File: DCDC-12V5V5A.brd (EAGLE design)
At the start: 40 x 23 mm, 32 parts, among them CN2 2828XX-2282834-2, CN3 2828XX-2282834-2, Q10 NMOSFET, Q9 NMOSFET, U1 LM3150MHX/NOPB

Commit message: Fixed some placement. Generated CAM files.
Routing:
- net 12V: track 15.4 -> 16.0 mm, vias 12 -> 13
- net GND: vias 36 -> 38
- net 5V: vias 17 -> 18
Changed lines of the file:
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@@
 <vertex x="13" y="20"/>
 <vertex x="15" y="20"/>
-<vertex x="15" y="22"/>
-<vertex x="9" y="22"/>
+<vertex x="15" y="21.7"/>
+<vertex x="9" y="21.7"/>
 <vertex x="9" y="17"/>
-<vertex x="7" y="15"/>
-<vertex x="2" y="15"/>
+<vertex x="6.5" y="14.5"/>
+<vertex x="2" y="14.5"/>
 <vertex x="2" y="12"/>
 <vertex x="3" y="12"/>
@@
 <vertex x="7" y="4"/>
 </polygon>
-<wire x1="18" y1="2.15" x2="17.55" y2="2.15" width="0.4064" layer="1"/>
-<wire x1="17.55" y1="2.15" x2="17.4" y2="2.3" width="0.4064" layer="1"/>
-<via x="17.4" y="2.3" extent="1-16" drill="0.35"/>
+<wire x1="18" y1="2.15" x2="17.15" y2="2.15" width="0.4064" layer="1"/>
+<wire x1="17.15" y1="2.15" x2="17.1" y2="2.2" width="0.4064" layer="1"/>
+<via x="17.1" y="2.2" extent="1-16" drill="0.35"/>
 <via x="14.2" y="5.7196375" extent="1-16" drill="0.35"/>
-<wire x1="17.4" y1="2.3" x2="15.7338" y2="3.9662" width="0.4064" layer="16"/>
-<wire x1="15.7338" y1="3.9662" x2="15.69605" y2="3.9662" width="0.4064" layer="16"/>
-<wire x1="15.69605" y1="3.9662" x2="14.831125" y2="4.831125" width="0.4064" layer="16"/>
-<wire x1="14.831125" y1="4.831125" x2="14.2" y2="5.46225" width="0.4064" layer="16"/>
+<wire x1="17.1" y1="2.2" x2="17.1" y2="2.56225" width="0.4064" layer="16"/>
+<wire x1="17.1" y1="2.56225" x2="14.931125" y2="4.731125" width="0.4064" layer="16"/>
+<wire x1="14.931125" y1="4.731125" x2="14.2" y2="5.46225" width="0.4064" layer="16"/>
 <wire x1="14.2" y1="5.46225" x2="14.2" y2="5.7196375" width="0.4064" layer="16"/>
 <wire x1="14.7" y1="6.315" x2="14.2" y2="5.815" width="0.4064" layer="1"/>
 <wire x1="14.2" y1="5.7196375" x2="14.2" y2="5.815" width="0.4064" layer="1"/>
 <wire x1="14.7" y1="6.315" x2="14.7" y2="7.115" width="0.4064" layer="1"/>
-<wire x1="14.831125" y1="4.831125" x2="14.831125" y2="4.512775" width="0.4064" layer="16"/>
-<wire x1="14.831125" y1="4.512775" x2="13.51835" y2="3.2" width="0.4064" layer="16"/>
-<wire x1="13.51835" y1="3.2" x2="12.7" y2="3.2" width="0.4064" layer="16"/>
-<wire x1="12.7" y1="3.2" x2="9" y2="6.9" width="0.4064" layer="16"/>
-<wire x1="9" y1="6.9" x2="9" y2="7" width="0.4064" layer="16"/>
+<wire x1="14.931125" y1="4.731125" x2="14.931125" y2="4.612775" width="0.4064" layer="16"/>
+<wire x1="14.931125" y1="4.612775" x2="13.51835" y2="3.2" width="0.4064" layer="16"/>
+<wire x1="13.51835" y1="3.2" x2="11.8" y2="3.2" width="0.4064" layer="16"/>
+<wire x1="11.8" y1="3.2" x2="9" y2="6" width="0.4064" layer="16"/>
+<wire x1="9" y1="6" x2="9" y2="7" width="0.4064" layer="16"/>
 <polygon width="0.254" layer="16" thermals="no">
 <vertex x="11" y="4"/>
@@
 <vertex x="3" y="12"/>
 <vertex x="2" y="12"/>
-<vertex x="2" y="15"/>
-<vertex x="7" y="15"/>
+<vertex x="2" y="14.5"/>
+<vertex x="6.5" y="14.5"/>
 <vertex x="9" y="17"/>
-<vertex x="9" y="22"/>
-<vertex x="15" y="22"/>
+<vertex x="9" y="21.7"/>
+<vertex x="15" y="21.7"/>
 <vertex x="15" y="20"/>
 <vertex x="11" y="16"/>
@@
 <via x="4" y="12" extent="1-16" drill="0.35"/>
 <via x="10" y="16" extent="1-16" drill="0.35"/>
+<via x="6" y="10" extent="1-16" drill="0.35"/>
 </signal>
 <signal name="GND" airwireshidden="yes">
@@
 <via x="12" y="14" extent="1-16" drill="0.35"/>
 <via x="17" y="5.6" extent="1-16" drill="0.35"/>
-<via x="20" y="16" extent="1-16" drill="0.35"/>
+<via x="20" y="17" extent="1-16" drill="0.35"/>
 <via x="20" y="11" extent="1-16" drill="0.35"/>
 <via x="20" y="5" extent="1-16" drill="0.35"/>
@@
 <via x="9" y="2" extent="1-16" drill="0.35"/>
 <via x="3" y="10" extent="1-16" drill="0.35"/>
+<via x="20" y="13" extent="1-16" drill="0.35"/>
+<via x="20" y="8" extent="1-16" drill="0.35"/>
 </signal>
 <signal name="5V" airwireshidden="yes">
@@
 <vertex x="37" y="15"/>
 <vertex x="38" y="14"/>
-<vertex x="38" y="12"/>
-<vertex x="37" y="12"/>
+<vertex x="38" y="11.4"/>
+<vertex x="36.4" y="11.4"/>
 <vertex x="35" y="10"/>
-<vertex x="35" y="6"/>
-<vertex x="33" y="4"/>
+<vertex x="35" y="6.3"/>
+<vertex x="33" y="4.3"/>
 <vertex x="33" y="3"/>
 <vertex x="21" y="3"/>
@@
 <vertex x="34" y="18"/>
 <vertex x="38" y="14"/>
-<vertex x="38" y="12"/>
-<vertex x="37" y="12"/>
+<vertex x="38" y="11.4"/>
+<vertex x="36.4" y="11.4"/>
 <vertex x="35" y="10"/>
-<vertex x="35" y="6"/>
-<vertex x="33" y="4"/>
+<vertex x="35" y="6.3"/>
+<vertex x="33" y="4.3"/>
 <vertex x="33" y="3"/>
 </polygon>
@@
 <via x="28" y="12" extent="1-16" drill="0.35"/>
 <via x="25" y="12" extent="1-16" drill="0.35"/>
+<via x="35" y="14" extent="1-16" drill="0.35"/>
 </signal>
 <signal name="BUCK_LG">
@@
 <vertex x="21" y="19"/>
 <vertex x="19" y="17"/>
-<vertex x="16" y="17"/>
-<vertex x="15" y="16"/>
+<vertex x="18" y="17"/>
+<vertex x="17" y="16"/>
 <vertex x="11" y="16"/>
 <vertex x="11" y="18"/>
@@
 <vertex x="17" y="22"/>
 </polygon>
-<wire x1="15.9944" y1="15.25270625" x2="15.9944" y2="16.2" width="0.4064" layer="1"/>
+<wire x1="16.0944" y1="15.15270625" x2="16.0944" y2="16.1" width="0.4064" layer="1"/>
 <wire x1="16.6606" y1="14.58650625" x2="16.6606" y2="12.8956" width="0.4064" layer="1"/>
 <wire x1="16.65" y1="12.885" x2="16.6606" y2="12.8956" width="0.4064" layer="1"/>
-<wire x1="16.6606" y1="14.58650625" x2="15.9944" y2="15.25270625" width="0.4064" layer="1"/>
-<wire x1="15.9944" y1="16.2" x2="15.1944" y2="17" width="0.4064" layer="1"/>
-<wire x1="15.1944" y1="17" x2="15" y2="17" width="0.4064" layer="1"/>
+<wire x1="16.6606" y1="14.58650625" x2="16.0944" y2="15.15270625" width="0.4064" layer="1"/>
+<wire x1="16.0944" y1="16.1" x2="15.4" y2="16.7944" width="0.4064" layer="1"/>
+<wire x1="15.4" y1="16.7944" x2="15.4" y2="16.8" width="0.4064" layer="1"/>
 </signal>
 <signal name="N$9">
@@
 <wire x1="15.6" y1="5" x2="12.15" y2="5" width="0.3048" layer="1"/>
 <wire x1="12.15" y1="5" x2="12" y2="5.15" width="0.3048" layer="1"/>
-<wire x1="10" y1="11.125" x2="11" y2="10.125" width="0.3048" layer="1"/>
-<wire x1="11" y1="6.15" x2="12" y2="5.15" width="0.3048" layer="1"/>
-<wire x1="11" y1="10.125" x2="11" y2="6.15" width="0.3048" layer="1"/>
+<wire x1="10" y1="11.125" x2="11.1" y2="10.025" width="0.3048" layer="1"/>
+<wire x1="11.1" y1="6.05" x2="12" y2="5.15" width="0.3048" layer="1"/>
+<wire x1="11.1" y1="10.025" x2="11.1" y2="6.05" width="0.3048" layer="1"/>
 </signal>
 <signal name="N$16">
 <contactref element="U1" pad="6"/>
 <contactref element="C42" pad="2"/>
-<wire x1="17.64876875" y1="8.1398" x2="18.25123125" y2="8.1398" width="0.3048" layer="1"/>
-<wire x1="17.3" y1="7.115" x2="17.3" y2="7.79103125" width="0.3048" layer="1"/>
-<wire x1="17.64876875" y1="8.1398" x2="17.3" y2="7.79103125" width="0.3048" layer="1"/>
+<wire x1="17.54876875" y1="8.1398" x2="18.25123125" y2="8.1398" width="0.3048" layer="1"/>
+<wire x1="17.3" y1="7.115" x2="17.3" y2="7.89103125" width="0.3048" layer="1"/>
+<wire x1="17.54876875" y1="8.1398" x2="17.3" y2="7.89103125" width="0.3048" layer="1"/>
 <wire x1="18.25123125" y1="8.1398" x2="18.5" y2="7.89103125" width="0.3048" layer="1"/>
 <wire x1="18.5" y1="7.89103125" x2="18.5" y2="5.375" width="0.3048" layer="1"/>
@@
 <wire x1="16" y1="3.875" x2="16.3" y2="4.175" width="0.3048" layer="1"/>
 <via x="16.3" y="4.6" extent="1-16" drill="0.35"/>
-<wire x1="15.35" y1="7.115" x2="15.35" y2="6.115" width="0.3048" layer="1"/>
-<wire x1="15.35" y1="6.115" x2="15.311375" y2="6.076375" width="0.3048" layer="1"/>
-<wire x1="15.311375" y1="6.076375" x2="15.311375" y2="5.888625" width="0.3048" layer="1"/>
-<wire x1="15.311375" y1="5.888625" x2="15.211375" y2="5.788625" width="0.3048" layer="1"/>
+<wire x1="15.35" y1="7.115" x2="15.35" y2="5.92725" width="0.3048" layer="1"/>
+<wire x1="15.35" y1="5.92725" x2="15.211375" y2="5.788625" width="0.3048" layer="1"/>
 <via x="15.211375" y="5.788625" extent="1-16" drill="0.35"/>
 <wire x1="15.211375" y1="5.788625" x2="16.3" y2="4.7" width="0.3048" layer="16"/>
@@
 <wire x1="13.4" y1="15.4" x2="12.7" y2="15.4" width="0.3048" layer="16"/>
 <via x="12.7" y="15.4" extent="1-16" drill="0.35"/>
-<wire x1="12.7" y1="15.4" x2="12.425" y2="15.125" width="0.3048" layer="1"/>
-<wire x1="12.425" y1="15.125" x2="12" y2="15.125" width="0.3048" layer="1"/>
+<wire x1="12.7" y1="15.4" x2="12.675" y2="15.425" width="0.3048" layer="1"/>
+<wire x1="12.675" y1="15.425" x2="12.3" y2="15.425" width="0.3048" layer="1"/>
+<wire x1="12.3" y1="15.425" x2="12" y2="15.125" width="0.3048" layer="1"/>
 </signal>
 <signal name="N$8">

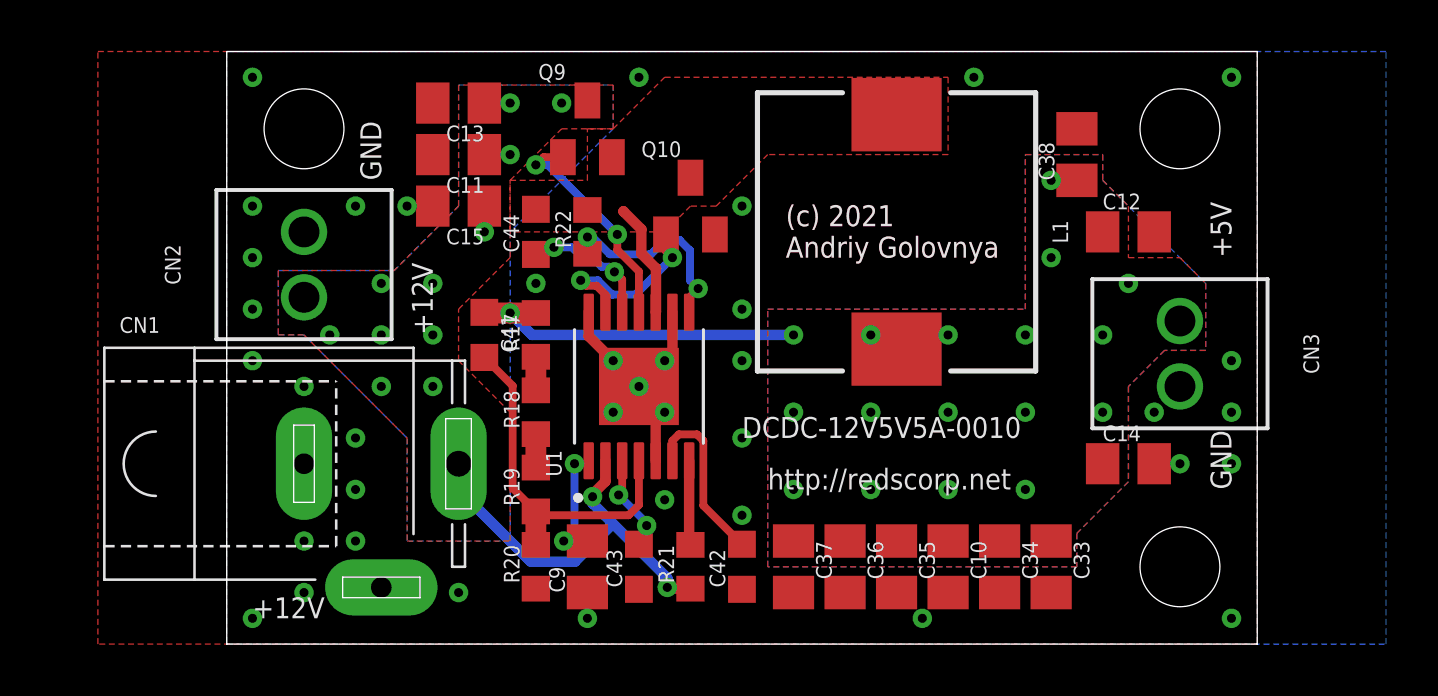
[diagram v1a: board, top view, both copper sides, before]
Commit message: Exchanged MOSFETs for bigger once. Generated CAM files. Generated BoM and PnP files.
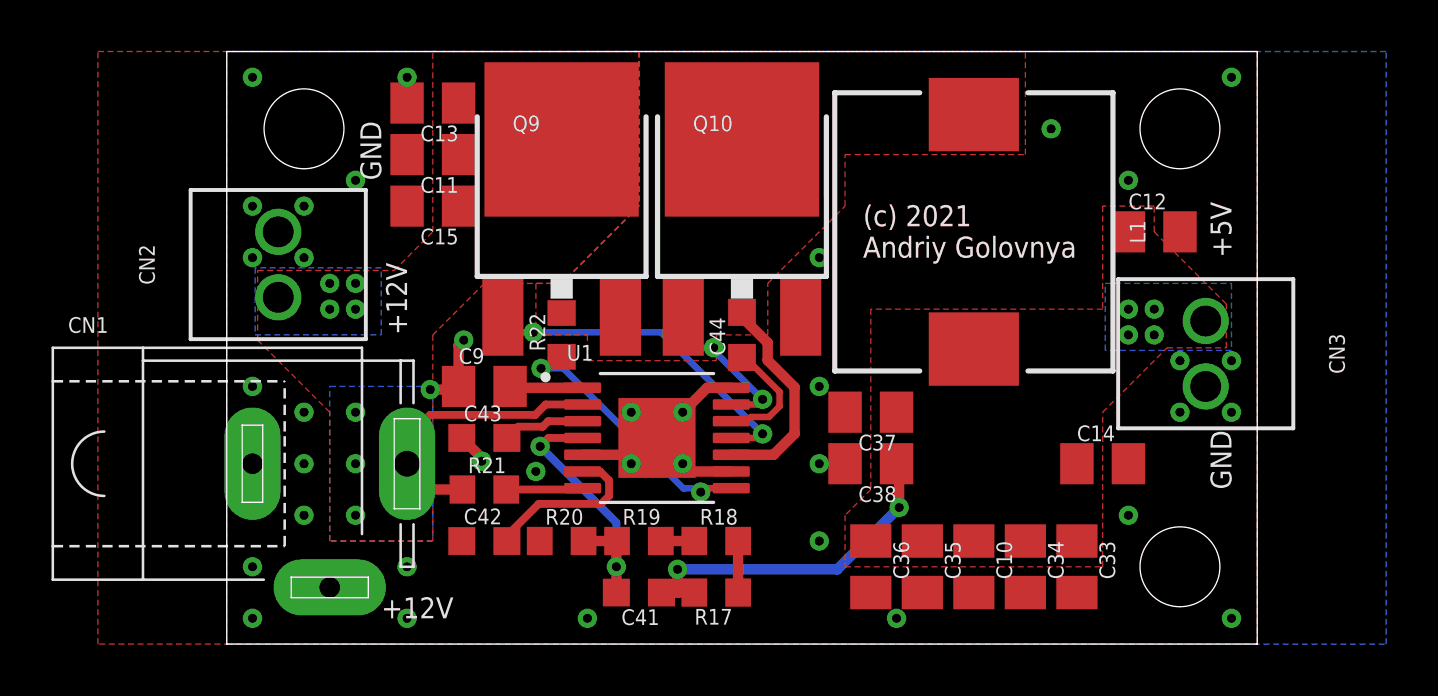
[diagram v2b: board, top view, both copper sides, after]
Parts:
- Q10, Q9: device Transistor:SOT23 -> BeagleBone_Blue_R3:DPAK
- moved C38 14.4 mm to (25.0, 7.00), turned to 180 degrees
- moved R17 12.2 mm to (19.0, 2.00), turned to 180 degrees
- moved C41 11.7 mm to (16.0, 2.00), turned to 180 degrees
- moved C42 10.0 mm to (10.0, 4.00), turned to 0 degrees
- moved C44 8.94 mm to (20.0, 12.0)
- moved R18 8.60 mm to (19.0, 4.00), turned to 0 degrees
- moved R21 8.54 mm to (10.0, 6.00), turned to 0 degrees
- moved C9 8.06 mm to (10.0, 10.0), turned to 0 degrees
- moved C43 7.81 mm to (10.0, 8.00), turned to 0 degrees
- moved C37 6.71 mm to (25.0, 9.00), turned to 180 degrees
- moved R19 4.47 mm to (16.0, 4.00), turned to 0 degrees
- moved R22 4.12 mm to (13.0, 12.0)
- moved L1 3.00 mm to (29.0, 16.0)
- moved Q10 2.24 mm to (20.0, 18.0)
- moved Q9 2.24 mm to (13.0, 18.0)
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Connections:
- net 12V: now also Q9.4; no longer Q9.3
- net BUCK_SW: now also Q10.4, Q9.3; no longer Q10.3, Q9.2
- net GND: now also Q10.3; no longer Q10.2
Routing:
- net 12V: track 16.0 -> 10.9 mm, vias 13 -> 7
- net BUCK_HG: track 8.82 -> 13.3 mm
- net GND: track 6.32 -> 10.6 mm
- net BUCK_SW: track 4.44 -> 8.35 mm
- net BUCK_FB: track 14.0 -> 11.0 mm, vias 0 -> 2
- net N$8: track 7.98 -> 10.4 mm
- net N$19: track 4.69 -> 2.84 mm, vias 2 -> 0
- net BUCK_LG: track 7.26 -> 6.23 mm
- net N$9: track 1.30 -> 2.00 mm
- net N$18: track 3.87 -> 3.21 mm, vias 2 -> 0
- net N$23: track 5.26 -> 4.68 mm, vias 2 -> 0
- net 5V: track 13.4 -> 13.5 mm, vias 18 -> 6

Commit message: Added indication LED. Generated CAM files. Generated BoM and PnP files.
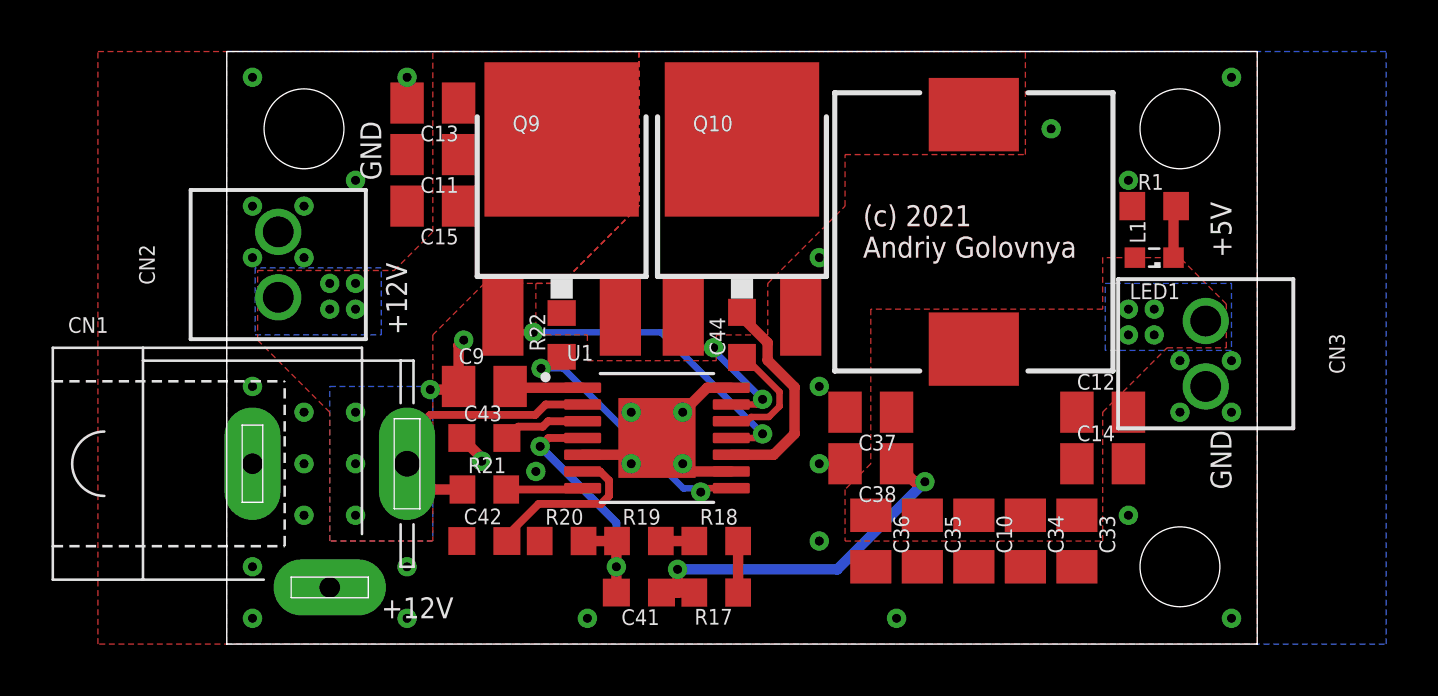
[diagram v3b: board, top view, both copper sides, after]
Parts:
- added LED1: GREEN, led:SML0603
- added R1: 3k, rcl:R0603
- moved C12 7.28 mm to (34.0, 9.00)
- moved C10 1.00 mm to (29.0, 4.00)
- moved C33 1.00 mm to (33.0, 4.00)
- moved C34 1.00 mm to (31.0, 4.00)
- moved C35 1.00 mm to (27.0, 4.00)
- moved C36 1.00 mm to (25.0, 4.00)
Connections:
- new net N$1: LED1.C, R1.2
- net 5V: now also LED1.A
- net GND: now also R1.1
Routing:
- net N$1: track 0.00 -> 2.04 mm
- net 5V: track 13.5 -> 14.6 mm
